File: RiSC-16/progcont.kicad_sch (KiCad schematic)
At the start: 9 parts, among them U19 74LS257, U20 74LS257, U3 74LS283, U5 74LS161

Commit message: Added a custom symbol for the AM29705. Reworked to use it in two different approaches.
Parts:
- renumbered C4 to C11, C5 to C12, C11 to C13, C12 to C14, R3 to R2, U3 to U11, U5 to U12, U19 to U13, U20 to U14
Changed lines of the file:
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@@
 		(dnp no)
 		(fields_autoplaced yes)
-		(property "Reference" "#PWR010"
+		(property "Reference" "#PWR027"
 			(at 204.47 33.02 0)
 			(effects
@@
 			(project "RiSC-16"
 				(path "/09ce4153-429f-4803-b069-3af485a81dd6/fa2f7088-dabe-4df0-996a-fa944d833eff"
-					(reference "#PWR010")
+					(reference "#PWR027")
 					(unit 1)
 				)
@@
 		(dnp no)
 		(fields_autoplaced yes)
-		(property "Reference" "#PWR09"
+		(property "Reference" "#PWR037"
 			(at 177.8 163.83 0)
 			(effects
@@
 			(project "RiSC-16"
 				(path "/09ce4153-429f-4803-b069-3af485a81dd6/fa2f7088-dabe-4df0-996a-fa944d833eff"
-					(reference "#PWR09")
+					(reference "#PWR037")
 					(unit 1)
 				)
@@
 		(dnp no)
 		(fields_autoplaced yes)
-		(property "Reference" "#PWR035"
+		(property "Reference" "#PWR030"
 			(at 185.42 36.83 0)
 			(effects
@@
 			(project "RiSC-16"
 				(path "/09ce4153-429f-4803-b069-3af485a81dd6/fa2f7088-dabe-4df0-996a-fa944d833eff"
-					(reference "#PWR035")
+					(reference "#PWR030")
 					(unit 1)
 				)
@@
 		(dnp no)
 		(fields_autoplaced yes)
-		(property "Reference" "C5"
+		(property "Reference" "C12"
 			(at 193.04 153.7969 0)
 			(effects
@@
 			(project "RiSC-16"
 				(path "/09ce4153-429f-4803-b069-3af485a81dd6/fa2f7088-dabe-4df0-996a-fa944d833eff"
-					(reference "C5")
+					(reference "C12")
 					(unit 1)
 				)
@@
 		(dnp no)
 		(fields_autoplaced yes)
-		(property "Reference" "U19"
+		(property "Reference" "U13"
 			(at 85.9633 34.29 0)
 			(effects
@@
 			(project "RiSC-16"
 				(path "/09ce4153-429f-4803-b069-3af485a81dd6/fa2f7088-dabe-4df0-996a-fa944d833eff"
-					(reference "U19")
+					(reference "U13")
 					(unit 1)
 				)
@@
 		(dnp no)
 		(fields_autoplaced yes)
-		(property "Reference" "#PWR034"
+		(property "Reference" "#PWR029"
 			(at 124.46 38.1 0)
 			(effects
@@
 			(project "RiSC-16"
 				(path "/09ce4153-429f-4803-b069-3af485a81dd6/fa2f7088-dabe-4df0-996a-fa944d833eff"
-					(reference "#PWR034")
+					(reference "#PWR029")
 					(unit 1)
 				)
@@
 		(dnp no)
 		(fields_autoplaced yes)
-		(property "Reference" "#PWR036"
+		(property "Reference" "#PWR031"
 			(at 204.47 76.2 0)
 			(effects
@@
 			(project "RiSC-16"
 				(path "/09ce4153-429f-4803-b069-3af485a81dd6/fa2f7088-dabe-4df0-996a-fa944d833eff"
-					(reference "#PWR036")
+					(reference "#PWR031")
 					(unit 1)
 				)
@@
 		(dnp no)
 		(fields_autoplaced yes)
-		(property "Reference" "C11"
+		(property "Reference" "C13"
 			(at 205.74 153.7969 0)
 			(effects
@@
 			(project "RiSC-16"
 				(path "/09ce4153-429f-4803-b069-3af485a81dd6/fa2f7088-dabe-4df0-996a-fa944d833eff"
-					(reference "C11")
+					(reference "C13")
 					(unit 1)
 				)
@@
 		(dnp no)
 		(fields_autoplaced yes)
-		(property "Reference" "U20"
+		(property "Reference" "U14"
 			(at 206.6133 83.82 0)
 			(effects
@@
 			(project "RiSC-16"
 				(path "/09ce4153-429f-4803-b069-3af485a81dd6/fa2f7088-dabe-4df0-996a-fa944d833eff"
-					(reference "U20")
+					(reference "U14")
 					(unit 1)
 				)
@@
 		(dnp no)
 		(fields_autoplaced yes)
-		(property "Reference" "C4"
+		(property "Reference" "C11"
 			(at 180.34 153.7969 0)
 			(effects
@@
 			(project "RiSC-16"
 				(path "/09ce4153-429f-4803-b069-3af485a81dd6/fa2f7088-dabe-4df0-996a-fa944d833eff"
-					(reference "C4")
+					(reference "C11")
 					(unit 1)
 				)
@@
 		(dnp no)
 		(fields_autoplaced yes)
-		(property "Reference" "#PWR040"
+		(property "Reference" "#PWR035"
 			(at 204.47 138.43 0)
 			(effects
@@
 			(project "RiSC-16"
 				(path "/09ce4153-429f-4803-b069-3af485a81dd6/fa2f7088-dabe-4df0-996a-fa944d833eff"
-					(reference "#PWR040")
+					(reference "#PWR035")
 					(unit 1)
 				)
@@
 		(dnp no)
 		(fields_autoplaced yes)
-		(property "Reference" "R3"
+		(property "Reference" "R2"
 			(at 109.22 27.94 90)
 			(effects
@@
 			(project "RiSC-16"
 				(path "/09ce4153-429f-4803-b069-3af485a81dd6/fa2f7088-dabe-4df0-996a-fa944d833eff"
-					(reference "R3")
+					(reference "R2")
 					(unit 1)
 				)
@@
 		(dnp no)
 		(fields_autoplaced yes)
-		(property "Reference" "U5"
+		(property "Reference" "U12"
 			(at 126.6033 34.29 0)
 			(effects
@@
 			(project "RiSC-16"
 				(path "/09ce4153-429f-4803-b069-3af485a81dd6/fa2f7088-dabe-4df0-996a-fa944d833eff"
-					(reference "U5")
+					(reference "U12")
 					(unit 1)
 				)
@@
 		(dnp no)
 		(fields_autoplaced yes)
-		(property "Reference" "#PWR07"
+		(property "Reference" "#PWR036"
 			(at 177.8 156.21 0)
 			(effects
@@
 			(project "RiSC-16"
 				(path "/09ce4153-429f-4803-b069-3af485a81dd6/fa2f7088-dabe-4df0-996a-fa944d833eff"
-					(reference "#PWR07")
+					(reference "#PWR036")
 					(unit 1)
 				)
@@
 		(dnp no)
 		(fields_autoplaced yes)
-		(property "Reference" "U3"
+		(property "Reference" "U11"
 			(at 206.6133 29.21 0)
 			(effects
@@
 			(project "RiSC-16"
 				(path "/09ce4153-429f-4803-b069-3af485a81dd6/fa2f7088-dabe-4df0-996a-fa944d833eff"
-					(reference "U3")
+					(reference "U11")
 					(unit 1)
 				)
@@
 		(dnp no)
 		(fields_autoplaced yes)
-		(property "Reference" "#PWR038"
+		(property "Reference" "#PWR033"
 			(at 83.82 88.9 0)
 			(effects
@@
 			(project "RiSC-16"
 				(path "/09ce4153-429f-4803-b069-3af485a81dd6/fa2f7088-dabe-4df0-996a-fa944d833eff"
-					(reference "#PWR038")
+					(reference "#PWR033")
 					(unit 1)
 				)
@@
 		(dnp no)
 		(fields_autoplaced yes)
-		(property "Reference" "#PWR037"
+		(property "Reference" "#PWR032"
 			(at 124.46 81.28 0)
 			(effects
@@
 			(project "RiSC-16"
 				(path "/09ce4153-429f-4803-b069-3af485a81dd6/fa2f7088-dabe-4df0-996a-fa944d833eff"
-					(reference "#PWR037")
+					(reference "#PWR032")
 					(unit 1)
 				)
@@
 		(dnp no)
 		(fields_autoplaced yes)
-		(property "Reference" "C12"
+		(property "Reference" "C14"
 			(at 218.44 153.7969 0)
 			(effects
@@
 			(project "RiSC-16"
 				(path "/09ce4153-429f-4803-b069-3af485a81dd6/fa2f7088-dabe-4df0-996a-fa944d833eff"
-					(reference "C12")
+					(reference "C14")
 					(unit 1)
 				)
@@
 		(dnp no)
 		(fields_autoplaced yes)
-		(property "Reference" "#PWR033"
+		(property "Reference" "#PWR028"
 			(at 83.82 38.1 0)
 			(effects
@@
 			(project "RiSC-16"
 				(path "/09ce4153-429f-4803-b069-3af485a81dd6/fa2f7088-dabe-4df0-996a-fa944d833eff"
-					(reference "#PWR033")
+					(reference "#PWR028")
 					(unit 1)
 				)
@@
 		(dnp no)
 		(fields_autoplaced yes)
-		(property "Reference" "#PWR039"
+		(property "Reference" "#PWR034"
 			(at 204.47 87.63 0)
 			(effects
@@
 			(project "RiSC-16"
 				(path "/09ce4153-429f-4803-b069-3af485a81dd6/fa2f7088-dabe-4df0-996a-fa944d833eff"
-					(reference "#PWR039")
-					(unit 1)
-				)
+					(reference "#PWR034")
+					(unit 1)
+				)

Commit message: Check point of design.
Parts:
- renumbered C11 to C14, C12 to C15, C13 to C16, C14 to C17, R2 to R3, U11 to U14, U12 to U15, U13 to U16, U14 to U17
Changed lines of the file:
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@@
 		(dnp no)
 		(fields_autoplaced yes)
-		(property "Reference" "#PWR027"
+		(property "Reference" "#PWR033"
 			(at 204.47 33.02 0)
 			(effects
@@
 			(project "RiSC-16"
 				(path "/09ce4153-429f-4803-b069-3af485a81dd6/fa2f7088-dabe-4df0-996a-fa944d833eff"
-					(reference "#PWR027")
+					(reference "#PWR033")
 					(unit 1)
 				)
@@
 		(dnp no)
 		(fields_autoplaced yes)
-		(property "Reference" "#PWR037"
+		(property "Reference" "#PWR043"
 			(at 177.8 163.83 0)
 			(effects
@@
 			(project "RiSC-16"
 				(path "/09ce4153-429f-4803-b069-3af485a81dd6/fa2f7088-dabe-4df0-996a-fa944d833eff"
-					(reference "#PWR037")
+					(reference "#PWR043")
 					(unit 1)
 				)
@@
 		(dnp no)
 		(fields_autoplaced yes)
-		(property "Reference" "#PWR030"
+		(property "Reference" "#PWR036"
 			(at 185.42 36.83 0)
 			(effects
@@
 			(project "RiSC-16"
 				(path "/09ce4153-429f-4803-b069-3af485a81dd6/fa2f7088-dabe-4df0-996a-fa944d833eff"
-					(reference "#PWR030")
+					(reference "#PWR036")
 					(unit 1)
 				)
@@
 		(dnp no)
 		(fields_autoplaced yes)
-		(property "Reference" "C12"
+		(property "Reference" "C15"
 			(at 193.04 153.7969 0)
 			(effects
@@
 			(project "RiSC-16"
 				(path "/09ce4153-429f-4803-b069-3af485a81dd6/fa2f7088-dabe-4df0-996a-fa944d833eff"
-					(reference "C12")
+					(reference "C15")
 					(unit 1)
 				)
@@
 		(dnp no)
 		(fields_autoplaced yes)
-		(property "Reference" "U13"
+		(property "Reference" "U16"
 			(at 85.9633 34.29 0)
 			(effects
@@
 			(project "RiSC-16"
 				(path "/09ce4153-429f-4803-b069-3af485a81dd6/fa2f7088-dabe-4df0-996a-fa944d833eff"
-					(reference "U13")
+					(reference "U16")
 					(unit 1)
 				)
@@
 		(dnp no)
 		(fields_autoplaced yes)
-		(property "Reference" "#PWR029"
+		(property "Reference" "#PWR035"
 			(at 124.46 38.1 0)
 			(effects
@@
 			(project "RiSC-16"
 				(path "/09ce4153-429f-4803-b069-3af485a81dd6/fa2f7088-dabe-4df0-996a-fa944d833eff"
-					(reference "#PWR029")
+					(reference "#PWR035")
 					(unit 1)
 				)
@@
 		(dnp no)
 		(fields_autoplaced yes)
-		(property "Reference" "#PWR031"
+		(property "Reference" "#PWR037"
 			(at 204.47 76.2 0)
 			(effects
@@
 			(project "RiSC-16"
 				(path "/09ce4153-429f-4803-b069-3af485a81dd6/fa2f7088-dabe-4df0-996a-fa944d833eff"
-					(reference "#PWR031")
+					(reference "#PWR037")
 					(unit 1)
 				)
@@
 		(dnp no)
 		(fields_autoplaced yes)
-		(property "Reference" "C13"
+		(property "Reference" "C16"
 			(at 205.74 153.7969 0)
 			(effects
@@
 			(project "RiSC-16"
 				(path "/09ce4153-429f-4803-b069-3af485a81dd6/fa2f7088-dabe-4df0-996a-fa944d833eff"
-					(reference "C13")
+					(reference "C16")
 					(unit 1)
 				)
@@
 		(dnp no)
 		(fields_autoplaced yes)
-		(property "Reference" "U14"
+		(property "Reference" "U17"
 			(at 206.6133 83.82 0)
 			(effects
@@
 			(project "RiSC-16"
 				(path "/09ce4153-429f-4803-b069-3af485a81dd6/fa2f7088-dabe-4df0-996a-fa944d833eff"
-					(reference "U14")
+					(reference "U17")
 					(unit 1)
 				)
@@
 		(dnp no)
 		(fields_autoplaced yes)
-		(property "Reference" "C11"
+		(property "Reference" "C14"
 			(at 180.34 153.7969 0)
 			(effects
@@
 			(project "RiSC-16"
 				(path "/09ce4153-429f-4803-b069-3af485a81dd6/fa2f7088-dabe-4df0-996a-fa944d833eff"
-					(reference "C11")
+					(reference "C14")
 					(unit 1)
 				)
@@
 		(dnp no)
 		(fields_autoplaced yes)
-		(property "Reference" "#PWR035"
+		(property "Reference" "#PWR041"
 			(at 204.47 138.43 0)
 			(effects
@@
 			(project "RiSC-16"
 				(path "/09ce4153-429f-4803-b069-3af485a81dd6/fa2f7088-dabe-4df0-996a-fa944d833eff"
-					(reference "#PWR035")
+					(reference "#PWR041")
 					(unit 1)
 				)
@@
 		(dnp no)
 		(fields_autoplaced yes)
-		(property "Reference" "R2"
+		(property "Reference" "R3"
 			(at 109.22 27.94 90)
 			(effects
@@
 			(project "RiSC-16"
 				(path "/09ce4153-429f-4803-b069-3af485a81dd6/fa2f7088-dabe-4df0-996a-fa944d833eff"
-					(reference "R2")
+					(reference "R3")
 					(unit 1)
 				)
@@
 		(dnp no)
 		(fields_autoplaced yes)
-		(property "Reference" "U12"
+		(property "Reference" "U15"
 			(at 126.6033 34.29 0)
 			(effects
@@
 			(project "RiSC-16"
 				(path "/09ce4153-429f-4803-b069-3af485a81dd6/fa2f7088-dabe-4df0-996a-fa944d833eff"
-					(reference "U12")
+					(reference "U15")
 					(unit 1)
 				)
@@
 		(dnp no)
 		(fields_autoplaced yes)
-		(property "Reference" "#PWR036"
+		(property "Reference" "#PWR042"
 			(at 177.8 156.21 0)
 			(effects
@@
 			(project "RiSC-16"
 				(path "/09ce4153-429f-4803-b069-3af485a81dd6/fa2f7088-dabe-4df0-996a-fa944d833eff"
-					(reference "#PWR036")
+					(reference "#PWR042")
 					(unit 1)
 				)
@@
 		(dnp no)
 		(fields_autoplaced yes)
-		(property "Reference" "U11"
+		(property "Reference" "U14"
 			(at 206.6133 29.21 0)
 			(effects
@@
 			(project "RiSC-16"
 				(path "/09ce4153-429f-4803-b069-3af485a81dd6/fa2f7088-dabe-4df0-996a-fa944d833eff"
-					(reference "U11")
+					(reference "U14")
 					(unit 1)
 				)
@@
 		(dnp no)
 		(fields_autoplaced yes)
-		(property "Reference" "#PWR033"
+		(property "Reference" "#PWR039"
 			(at 83.82 88.9 0)
 			(effects
@@
 			(project "RiSC-16"
 				(path "/09ce4153-429f-4803-b069-3af485a81dd6/fa2f7088-dabe-4df0-996a-fa944d833eff"
-					(reference "#PWR033")
+					(reference "#PWR039")
 					(unit 1)
 				)
@@
 		(dnp no)
 		(fields_autoplaced yes)
-		(property "Reference" "#PWR032"
+		(property "Reference" "#PWR038"
 			(at 124.46 81.28 0)
 			(effects
@@
 			(project "RiSC-16"
 				(path "/09ce4153-429f-4803-b069-3af485a81dd6/fa2f7088-dabe-4df0-996a-fa944d833eff"
-					(reference "#PWR032")
+					(reference "#PWR038")
 					(unit 1)
 				)
@@
 		(dnp no)
 		(fields_autoplaced yes)
-		(property "Reference" "C14"
+		(property "Reference" "C17"
 			(at 218.44 153.7969 0)
 			(effects
@@
 			(project "RiSC-16"
 				(path "/09ce4153-429f-4803-b069-3af485a81dd6/fa2f7088-dabe-4df0-996a-fa944d833eff"
-					(reference "C14")
+					(reference "C17")
 					(unit 1)
 				)
@@
 		(dnp no)
 		(fields_autoplaced yes)
-		(property "Reference" "#PWR028"
+		(property "Reference" "#PWR034"
 			(at 83.82 38.1 0)
 			(effects
@@
 			(project "RiSC-16"
 				(path "/09ce4153-429f-4803-b069-3af485a81dd6/fa2f7088-dabe-4df0-996a-fa944d833eff"
-					(reference "#PWR028")
+					(reference "#PWR034")
 					(unit 1)
 				)
@@
 		(dnp no)
 		(fields_autoplaced yes)
-		(property "Reference" "#PWR034"
+		(property "Reference" "#PWR040"
 			(at 204.47 87.63 0)
 			(effects
@@
 			(project "RiSC-16"
 				(path "/09ce4153-429f-4803-b069-3af485a81dd6/fa2f7088-dabe-4df0-996a-fa944d833eff"
-					(reference "#PWR034")
-					(unit 1)
-				)
+					(reference "#PWR040")
+					(unit 1)
+				)

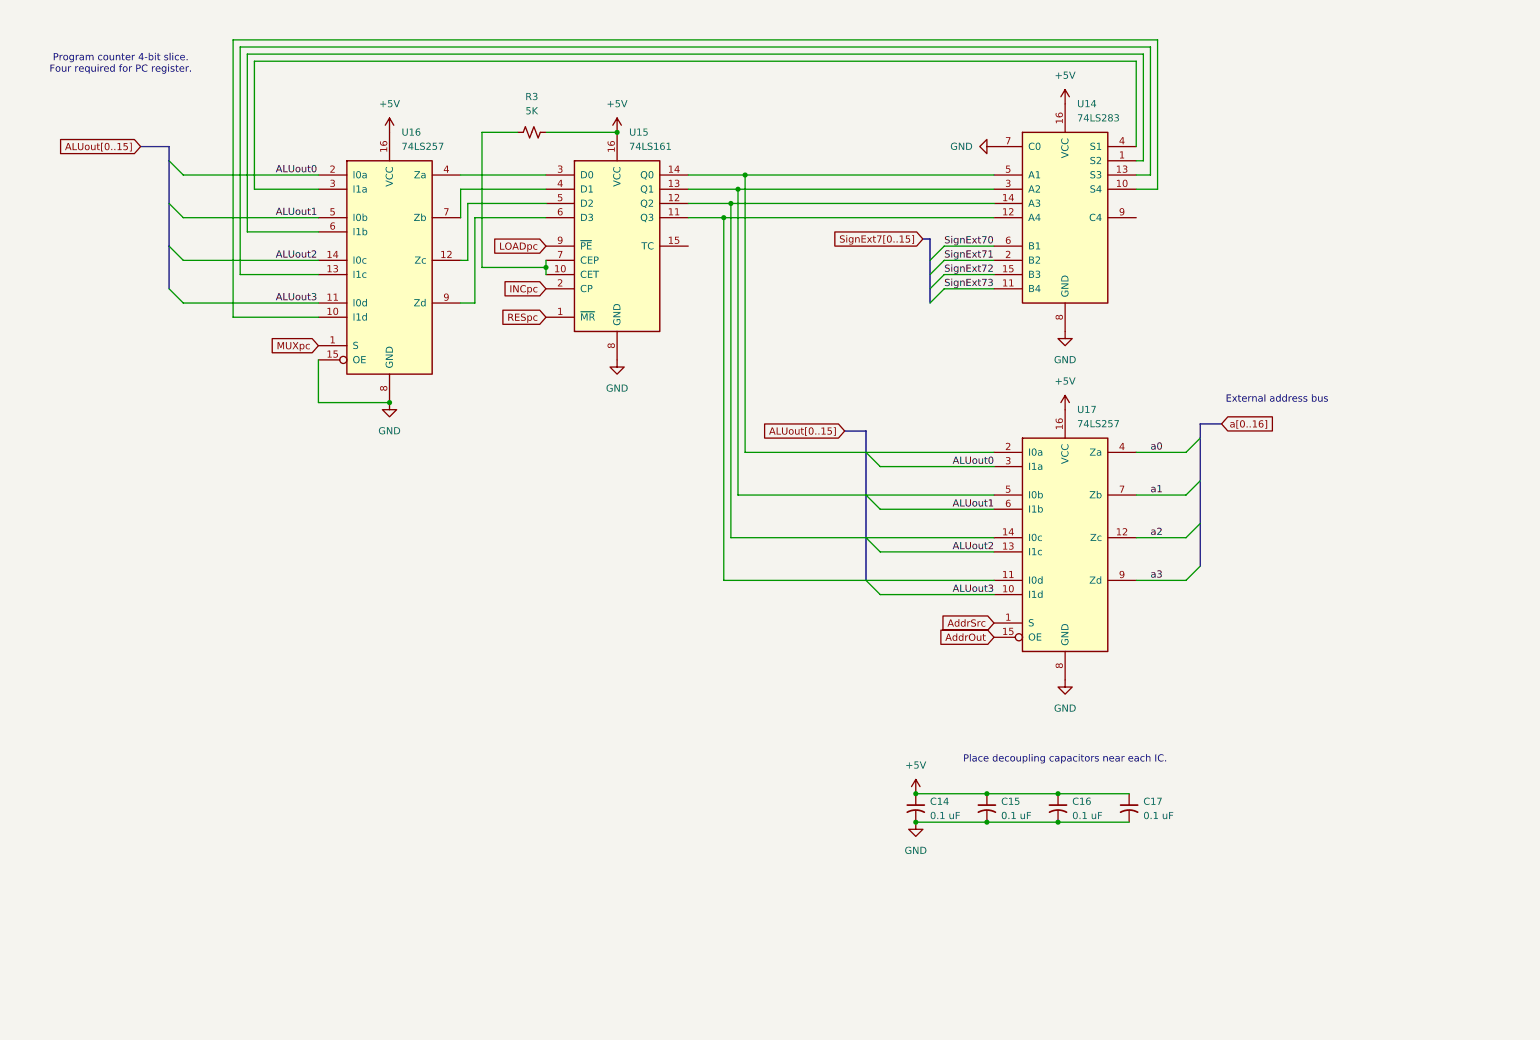
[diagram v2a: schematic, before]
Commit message: Moved and renamed pages.
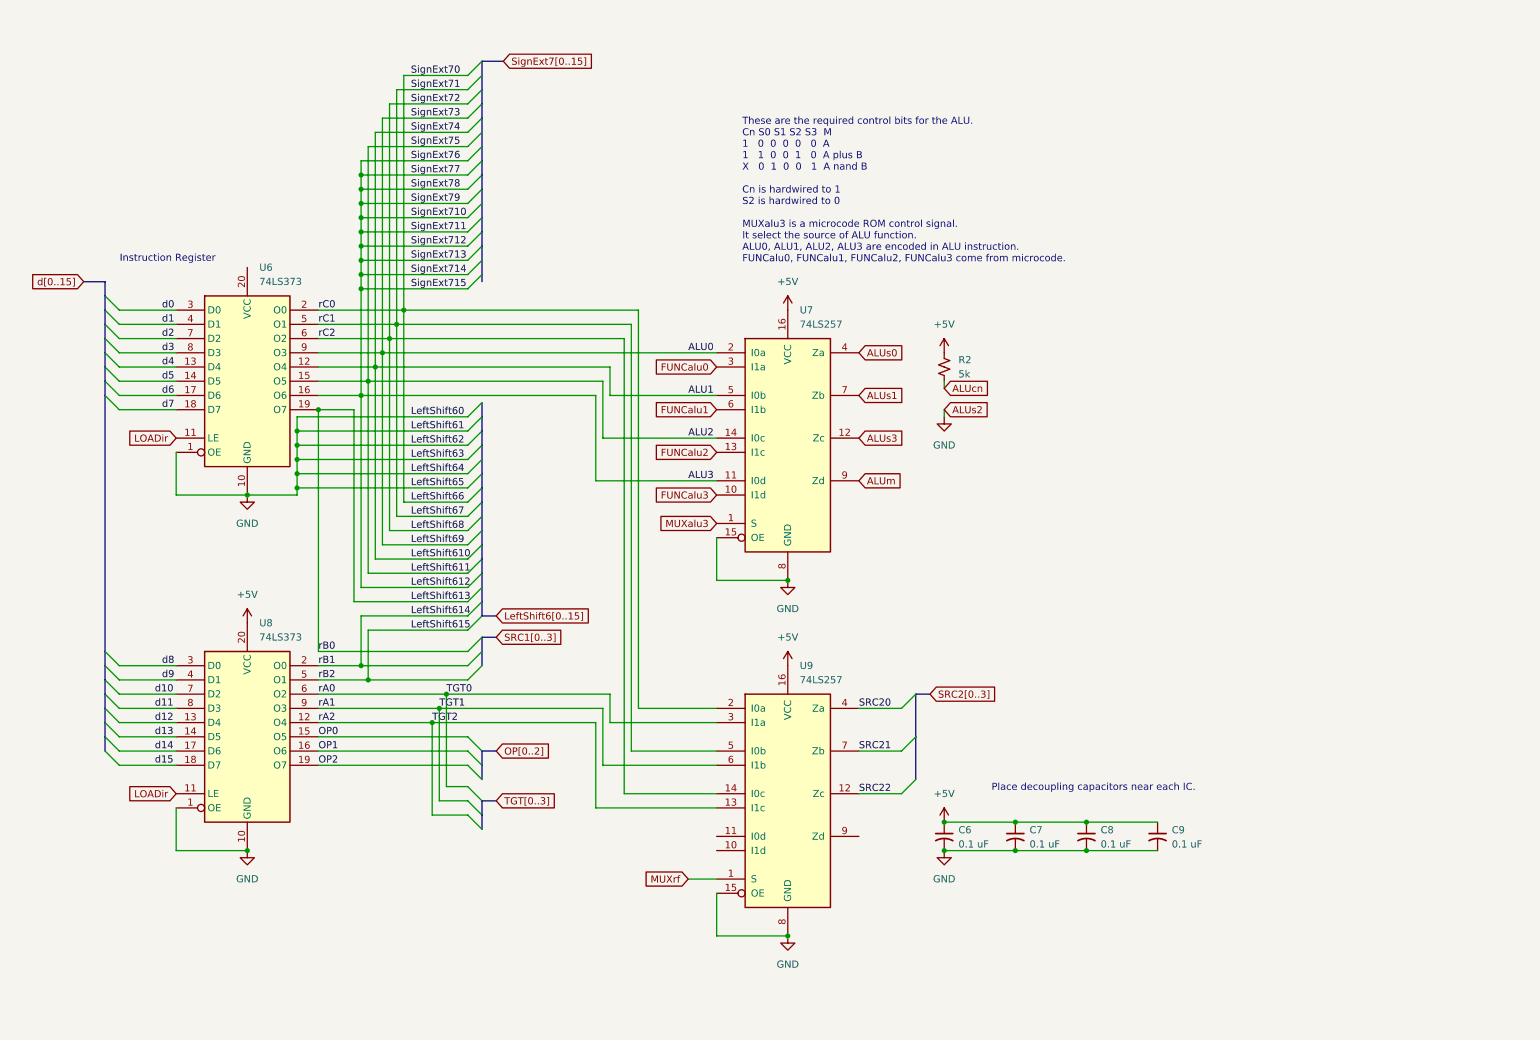
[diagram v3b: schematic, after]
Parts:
- removed C14, C15, C16, C17: 0.1 uF, symbol Device:C_Small_US
- removed R3: 5K, symbol Device:R_Small_US
- removed U14: 74LS283, symbol 74xx:74LS283
- removed U15: 74LS161, symbol 74xx:74LS161
- removed U16, U17: 74LS257, symbol 74xx:74LS257
- added C6, C7, C8, C9: 0.1 uF, symbol Device:C_Small_US
- added R2: 5k, symbol Device:R_Small_US
- added U6, U8: 74LS373, symbol 74xx:74LS373
- added U7, U9: 74LS257, symbol 74xx:74LS257
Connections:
- net +5V: now also C6.1, C7.1, C8.1, C9.1, R2.1, U7.16 (VCC), U8.20 (VCC), U9.16 (VCC)
- net GND: now also C6.2, C7.2, C8.2, C9.2, U6.1 (OE), U6.10 (GND), U7.15 (OE), U7.8 (GND), U8.1 (OE), U8.10 (GND), U9.15 (OE), U9.8 (GND)
- new net ALU0: U6.9 (O3), U7.2 (I0a)
- new net ALU1: U6.12 (O4), U7.5 (I0b)
- new net ALU2: U6.15 (O5), U7.14 (I0c)
- new net ALU3: U6.16 (O6), U7.11 (I0d)
- new net ALUcn: R2.2
- new net ALUm: U7.9 (Zd)
- new net ALUs0: U7.4 (Za)
- new net ALUs1: U7.7 (Zb)
- new net ALUs3: U7.12 (Zc)
- new net FUNCalu0: U7.3 (I1a)
- new net FUNCalu1: U7.6 (I1b)
- new net FUNCalu2: U7.13 (I1c)
- new net FUNCalu3: U7.10 (I1d)
- new net LOADir: U6.11 (LE), U8.11 (LE)
- new net LeftShift613: U6.19 (O7)
- new net LeftShift614: U8.2 (O0)
- new net LeftShift615: U8.5 (O1)
- new net LeftShift66: U6.2 (O0), U9.2 (I0a)
- new net LeftShift67: U6.5 (O1), U9.5 (I0b)
- new net LeftShift68: U6.6 (O2), U9.14 (I0c)
- new net MUXalu3: U7.1 (S)
- new net MUXrf: U9.1 (S)
- new net OP0: U8.15 (O5)
- new net OP1: U8.16 (O6)
- new net OP2: U8.19 (O7)
- new net SRC20: U9.4 (Za)
- new net SRC21: U9.7 (Zb)
- new net SRC22: U9.12 (Zc)
- new net TGT0: U8.6 (O2), U9.3 (I1a)
- new net TGT1: U8.9 (O3), U9.6 (I1b)
- new net TGT2: U8.12 (O4), U9.13 (I1c)
- new net d0: U6.3 (D0)
- new net d1: U6.4 (D1)
- new net d10: U8.7 (D2)
- new net d11: U8.8 (D3)
- new net d12: U8.13 (D4)
- new net d13: U8.14 (D5)
- new net d14: U8.17 (D6)
- new net d15: U8.18 (D7)
- new net d2: U6.7 (D2)
- new net d3: U6.8 (D3)
- new net d4: U6.13 (D4)
- new net d5: U6.14 (D5)
- new net d6: U6.17 (D6)
- new net d7: U6.18 (D7)
- new net d8: U8.3 (D0)
- new net d9: U8.4 (D1)
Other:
- note added: "Instruction Register"
- note added: "These are the required control bits for the ALU. Cn S0 S1 S2 S3 M 1 0 0 0 0 0 A 1 1 0 0 1 0 A plus B X 0 1 0 0 1 A nand B Cn is hardwired to 1 S2 is hardwired to 0 MUXalu3 is a microcode ROM control signal. It select the source of ALU function. ALU0, ALU1, ALU2, ALU3 are encoded in ALU instruction. FUNCalu0, FUNCalu1, FUNCalu2, FUNCalu3 come from microcode."
- note removed: "External address bus"
- note removed: "Program counter 4-bit slice. Four required for PC register."
